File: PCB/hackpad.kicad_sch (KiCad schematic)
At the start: 9 parts, among them SW1 SW_Push, SW2 SW_Push, SW3 SW_Push, SW4 SW_Push, U1 XIAO-RP2040-DIP

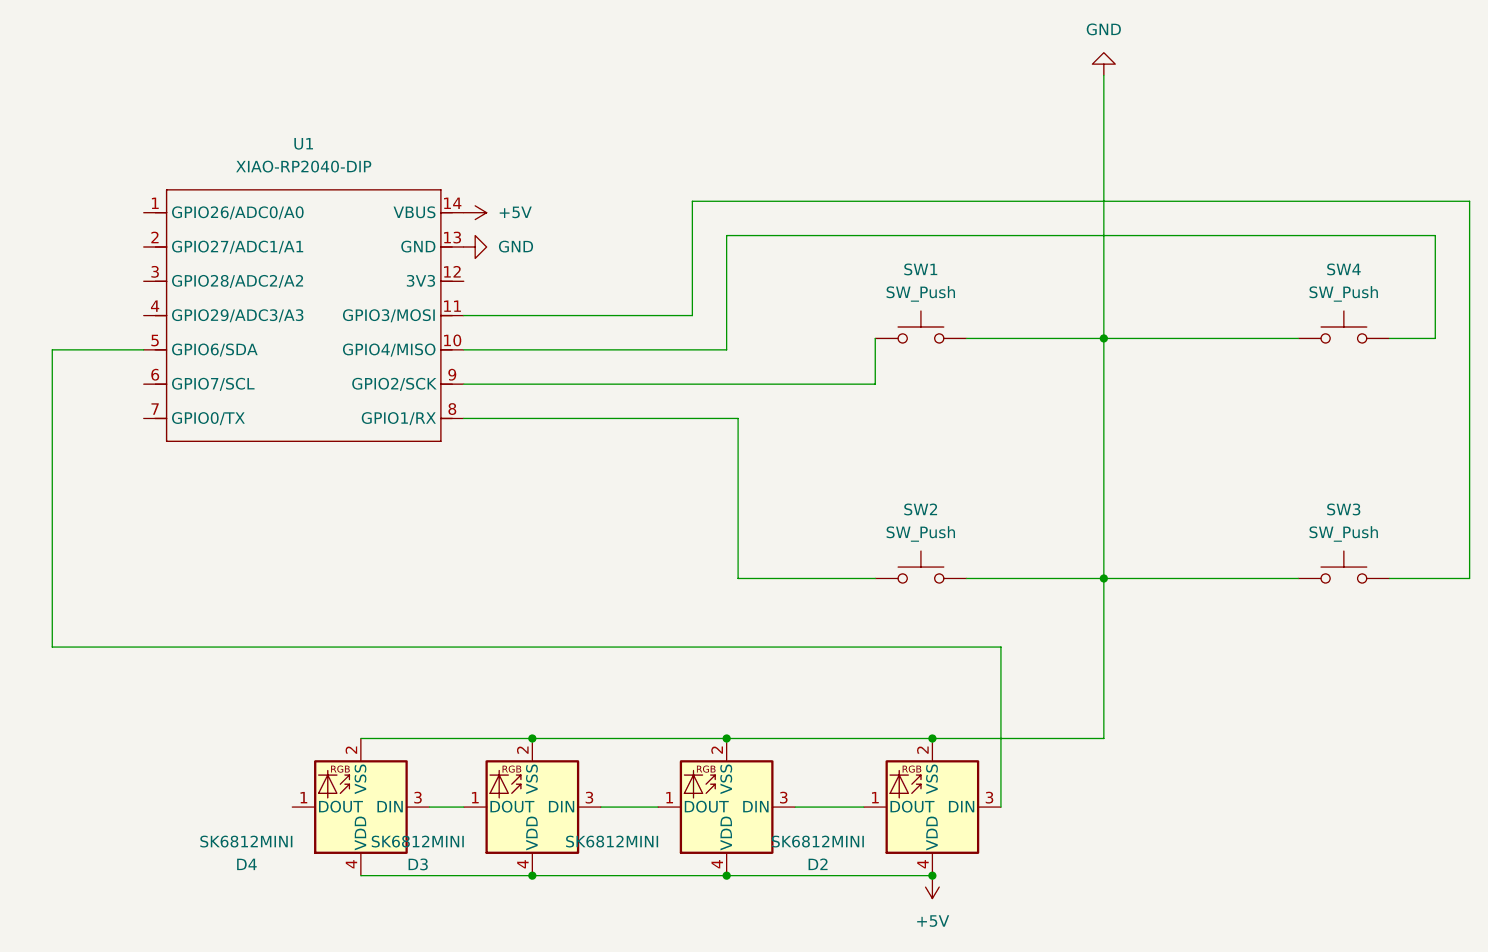
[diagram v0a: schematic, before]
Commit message: Added rotary-encoder
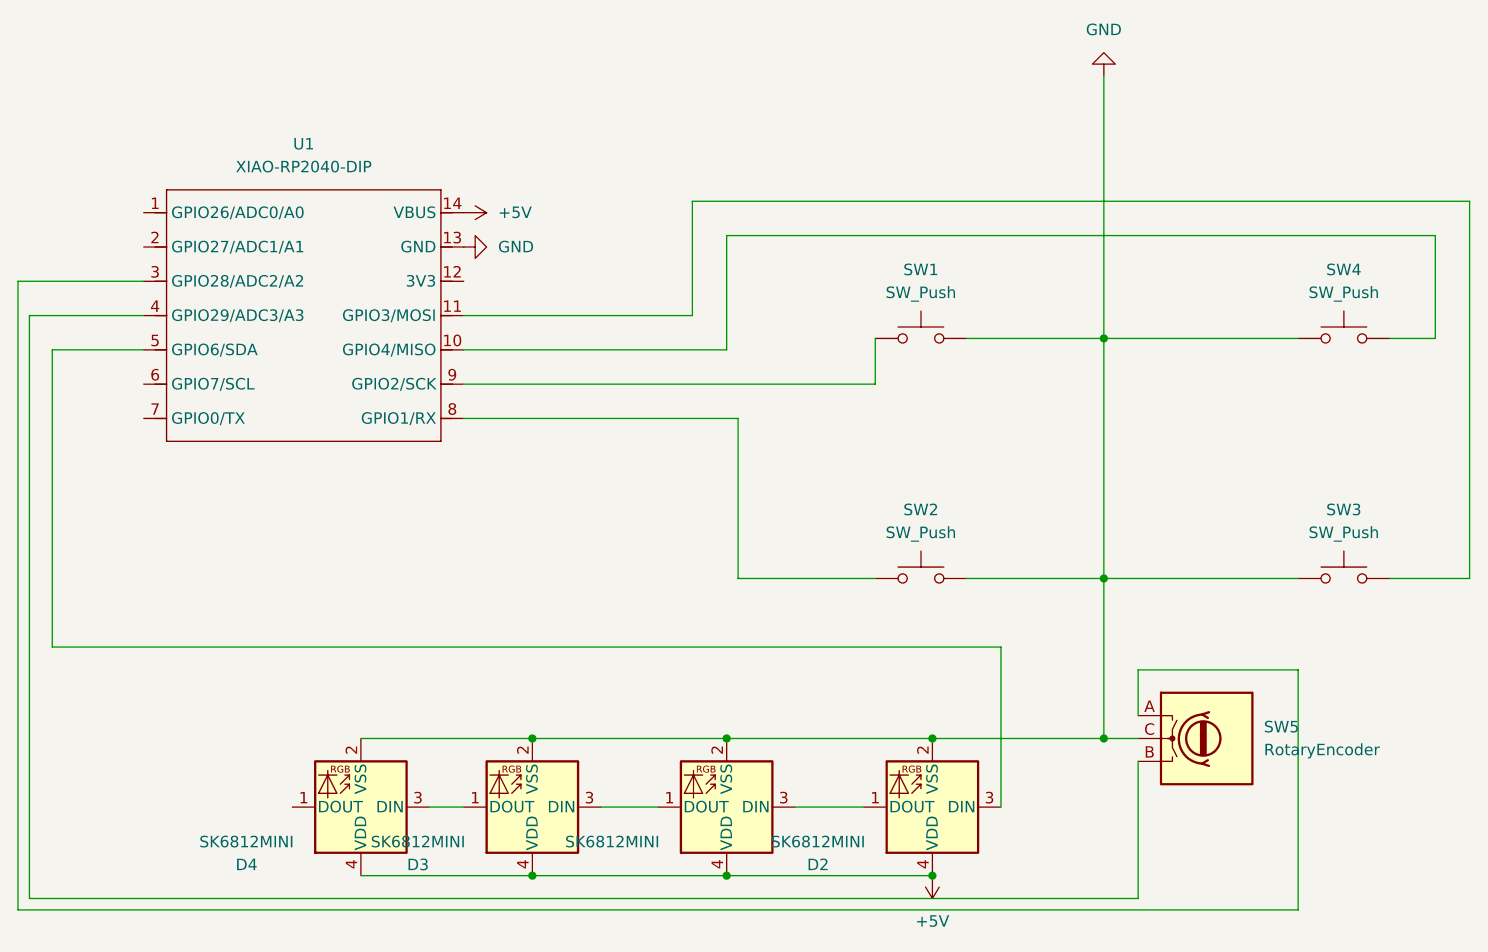
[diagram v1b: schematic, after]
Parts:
- added SW5: RotaryEncoder, Rotary_Encoder:RotaryEncoder_Alps_EC11E_Vertical_H20mm, symbol Device:RotaryEncoder
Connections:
- net GND: now also SW5.C
- net at U1.3 (GPIO28/ADC2/A2): now also SW5.A
- net at U1.4 (GPIO29/ADC3/A3): now also SW5.B
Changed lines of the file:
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@@
 	(paper "A4")
+	(junction
+		(at 139.7 104.14)
+		(diameter 0)
+		(color 0 0 0 0)
+	)
 	(junction
 		(at 76.2 119.38)
@@
 	(wire
 		(pts
+			(xy 161.29 96.52) (xy 161.29 123.19)
+		)
+		(stroke
+			(width 0)
+			(type default)
+		)
+	)
+	(wire
+		(pts
 			(xy 22.86 60.96) (xy 22.86 93.98)
 		)
@@
 	(wire
 		(pts
+			(xy 143.51 106.68) (xy 143.51 121.92)
+		)
+		(stroke
+			(width 0)
+			(type default)
+		)
+	)
+	(wire
+		(pts
 			(xy 139.7 59.69) (xy 139.7 86.36)
 		)
@@
 	(wire
 		(pts
+			(xy 20.32 57.15) (xy 33.02 57.15)
+		)
+		(stroke
+			(width 0)
+			(type default)
+		)
+	)
+	(wire
+		(pts
+			(xy 139.7 104.14) (xy 143.51 104.14)
+		)
+		(stroke
+			(width 0)
+			(type default)
+		)
+	)
+	(wire
+		(pts
 			(xy 90.17 111.76) (xy 83.82 111.76)
 		)
@@
 	(wire
 		(pts
+			(xy 161.29 123.19) (xy 19.05 123.19)
+		)
+		(stroke
+			(width 0)
+			(type default)
+		)
+	)
+	(wire
+		(pts
 			(xy 176.53 59.69) (xy 176.53 48.26)
 		)
@@
 	(wire
 		(pts
+			(xy 143.51 96.52) (xy 161.29 96.52)
+		)
+		(stroke
+			(width 0)
+			(type default)
+		)
+	)
+	(wire
+		(pts
 			(xy 128.27 93.98) (xy 128.27 111.76)
 		)
@@
 	(wire
 		(pts
+			(xy 19.05 53.34) (xy 33.02 53.34)
+		)
+		(stroke
+			(width 0)
+			(type default)
+		)
+	)
+	(wire
+		(pts
 			(xy 124.46 86.36) (xy 139.7 86.36)
 		)
@@
 	(wire
 		(pts
+			(xy 143.51 101.6) (xy 143.51 96.52)
+		)
+		(stroke
+			(width 0)
+			(type default)
+		)
+	)
+	(wire
+		(pts
 			(xy 114.3 59.69) (xy 114.3 64.77)
 		)
@@
 	(wire
 		(pts
+			(xy 143.51 121.92) (xy 20.32 121.92)
+		)
+		(stroke
+			(width 0)
+			(type default)
+		)
+	)
+	(wire
+		(pts
 			(xy 97.79 119.38) (xy 120.65 119.38)
 		)
@@
 		(pts
 			(xy 76.2 104.14) (xy 97.79 104.14)
+		)
+		(stroke
+			(width 0)
+			(type default)
+		)
+	)
+	(wire
+		(pts
+			(xy 19.05 53.34) (xy 19.05 123.19)
+		)
+		(stroke
+			(width 0)
+			(type default)
+		)
+	)
+	(wire
+		(pts
+			(xy 20.32 121.92) (xy 20.32 57.15)
 		)
 		(stroke
@@
 					(unit 1)
 				)
+			)
+		)
+	)
+	(symbol
+		(lib_id "Device:RotaryEncoder")
+		(at 151.13 104.14 0)
+		(unit 1)
+		(exclude_from_sim no)
+		(in_bom yes)
+		(on_board yes)
+		(dnp no)
+		(fields_autoplaced yes)
+		(property "Reference" "SW5"
+			(at 157.48 102.8699 0)
+			(effects
+				(font
+					(size 1.27 1.27)
+				)
+				(justify left)
+			)
+		)
+		(property "Value" "RotaryEncoder"
+			(at 157.48 105.4099 0)
+			(effects
+				(font
+					(size 1.27 1.27)
+				)
+				(justify left)
+			)
+		)
+		(property "Footprint" "Rotary_Encoder:RotaryEncoder_Alps_EC11E_Vertical_H20mm"
+			(at 147.32 100.076 0)
+			(effects
+				(font
+					(size 1.27 1.27)
+				)
+				(hide yes)
+			)
+		)
+		(property "Datasheet" "~"
+			(at 151.13 97.536 0)
+			(effects
+				(font
+					(size 1.27 1.27)
+				)
+				(hide yes)
+			)
+		)
+		(property "Description" "Rotary encoder, dual channel, incremental quadrate outputs"
+			(at 151.13 104.14 0)
+			(effects
+				(font
+					(size 1.27 1.27)
+				)
+				(hide yes)
+			)
+		)
+		(pin "A"
+		)
+		(pin "C"
+		)
+		(pin "B"
+		)
+		(instances
+			(project ""
+				(path "/ce49d2e9-1b2c-4fd2-8422-46e8816ca352"
+					(reference "SW5")
+					(unit 1)
+				)
